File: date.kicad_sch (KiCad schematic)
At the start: 4 parts, among them U1 MAX7219

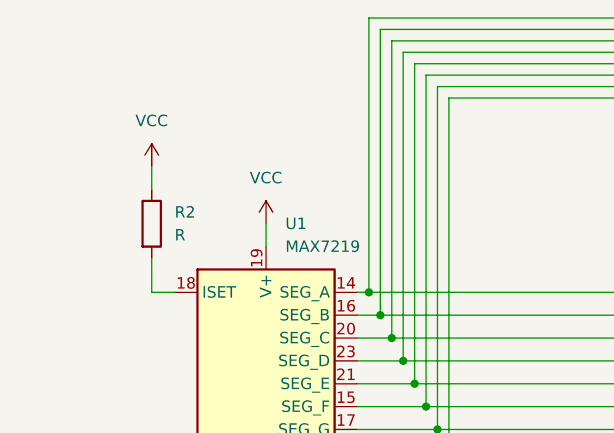
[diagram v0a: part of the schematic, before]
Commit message: Added VBUS and misc
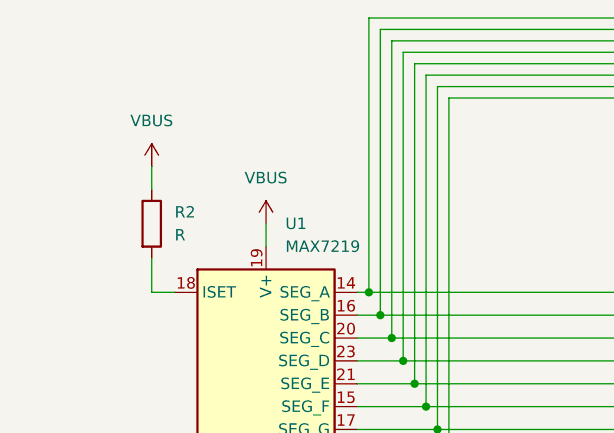
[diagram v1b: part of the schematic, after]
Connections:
- net VCC renamed VBUS
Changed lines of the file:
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@@
 	)
 	(symbol
-		(lib_id "power:VCC")
+		(lib_id "power:VBUS")
 		(at 71.12 67.31 0)
 		(unit 1)
@@
 		(dnp no)
 		(fields_autoplaced yes)
-		(property "Reference" "#PWR06"
+		(property "Reference" "#PWR03"
 			(at 71.12 71.12 0)
 			(effects
@@
 			)
 		)
-		(property "Value" "VCC"
+		(property "Value" "VBUS"
 			(at 71.12 62.23 0)
 			(effects
@@
 			)
 		)
-		(property "Description" "Power symbol creates a global label with name \"VCC\""
+		(property "Description" "Power symbol creates a global label with name \"VBUS\""
 			(at 71.12 67.31 0)
 			(effects
@@
 		)
 		(instances
-			(project ""
+			(project "reveil"
 				(path "/6015885c-867c-4e88-9a3e-de8167bfed74/9487cf58-7cf7-48e9-978c-ddf22de806a0"
-					(reference "#PWR06")
+					(reference "#PWR03")
 					(unit 1)
 				)
@@
 	)
 	(symbol
-		(lib_id "power:VCC")
+		(lib_id "power:VBUS")
 		(at 83.82 73.66 0)
 		(unit 1)
@@
 			)
 		)
-		(property "Value" "VCC"
+		(property "Value" "VBUS"
 			(at 83.82 68.58 0)
 			(effects
@@
 			)
 		)
-		(property "Description" "Power symbol creates a global label with name \"VCC\""
+		(property "Description" "Power symbol creates a global label with name \"VBUS\""
 			(at 83.82 73.66 0)
 			(effects
@@
 		)
 		(instances
-			(project ""
+			(project "reveil"
 				(path "/6015885c-867c-4e88-9a3e-de8167bfed74/9487cf58-7cf7-48e9-978c-ddf22de806a0"
 					(reference "#PWR05")

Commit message: tous les composants sont ajoutés et connecté dans le schema
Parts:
- R2: footprint (none) -> Resistor_THT:R_Axial_DIN0207_L6.3mm_D2.5mm_P7.62mm_Horizontal
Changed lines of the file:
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@@
 			)
 		)
-		(property "Footprint" ""
+		(property "Footprint" "Resistor_THT:R_Axial_DIN0207_L6.3mm_D2.5mm_P7.62mm_Horizontal"
 			(at 69.342 73.66 90)
 			(effects

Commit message: decoupling caps
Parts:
- added C1: 100nF, Capacitor_THT:C_Disc_D3.0mm_W1.6mm_P2.50mm, symbol Device:C
- added C2: 10uF, Capacitor_THT:CP_Radial_D7.5mm_P2.50mm, symbol Device:C_Polarized
- R2: value R -> 47K
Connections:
- net GND: now also C1.2, C2.2
- net VBUS: now also C1.1, C2.1
